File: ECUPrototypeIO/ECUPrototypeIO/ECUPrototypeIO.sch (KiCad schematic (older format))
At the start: 35 parts, among them SW2 MomentarySwitch, U1 LM358

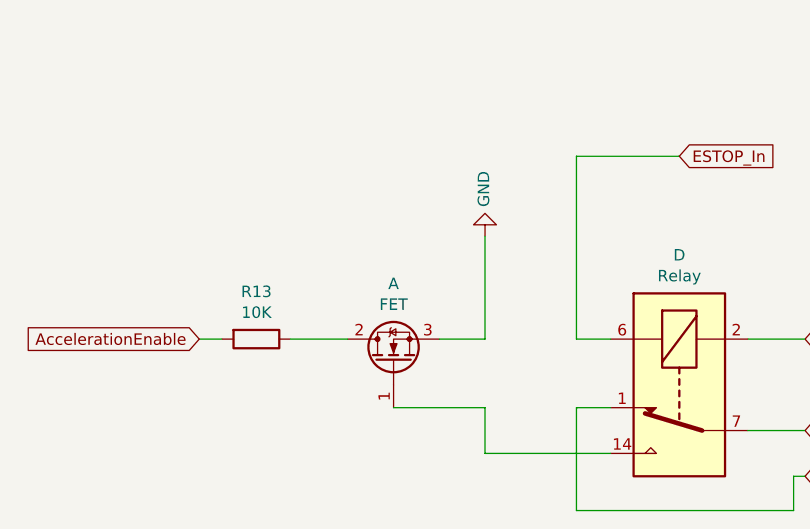
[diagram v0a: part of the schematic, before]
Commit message: Fixed the mosfet schematic
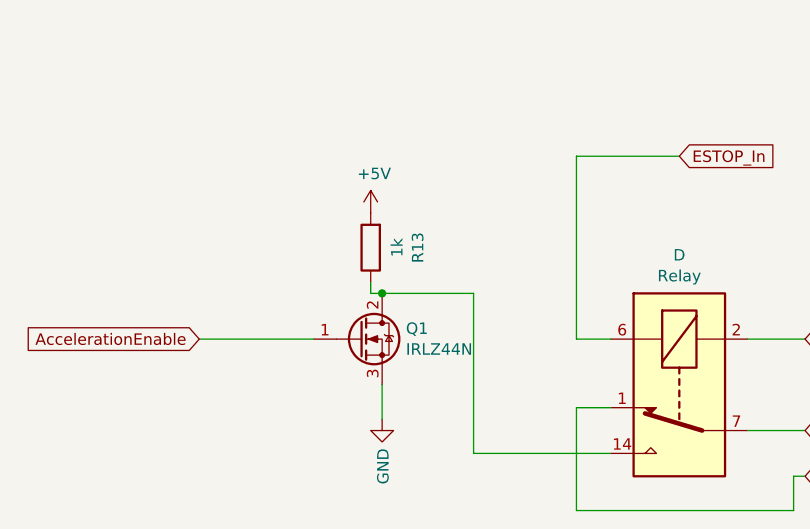
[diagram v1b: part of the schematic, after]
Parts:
- removed A: FET, Package_TO_SOT_THT:TO-220-3_Vertical, symbol Transistor_FET:IRF740
- added Q1: IRLZ44N, Package_TO_SOT_THT:TO-220-3_Vertical, symbol Transistor_FET:IRLZ44N
- R13: value 10K -> 1k
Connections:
- net labels added: +5V
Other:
- moved on the sheet: R13
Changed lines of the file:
@@
 L Device:R R13
 U 1 1 5E0710B8
-P 6950 8150
-F 0 "R13" V 6743 8150 50  0000 C CNN
-F 1 "10K" V 6834 8150 50  0000 C CNN
-F 2 "" V 6880 8150 50  0001 C CNN
-F 3 "~" H 6950 8150 50  0001 C CNN
-	1    6950 8150
-	0    1    1    0
+P 7450 7750
+F 0 "R13" V 7243 7750 50  0000 C CNN
+F 1 "1k" V 7334 7750 50  0000 C CNN
+F 2 "" V 7380 7750 50  0001 C CNN
+F 3 "~" H 7450 7750 50  0001 C CNN
+	1    7450 7750
+	-1   0    0    1
 $EndComp
 Text GLabel 6700 8150 0    50   Input ~ 0
 AccelerationEnable
-Wire Wire Line
-	6700 8150 6800 8150
 Text GLabel 8800 7350 2    50   Input ~ 0
 ESTOP_In
@@
 	8900 6450 9550 6450
 Connection ~ 8650 5750
-Wire Wire Line
-	7950 8650 8500 8650
 Text GLabel 9350 8550 2    50   Input ~ 0
 ACC_White
@@
 	11150 1450 11150 1300
 $Comp
-L Transistor_FET:IRF740 A
-U 1 1 5E2EE751
-P 7550 8250
-F 0 "A" V 7892 8250 50  0000 C CNN
-F 1 "FET" V 7801 8250 50  0000 C CNN
-F 2 "Package_TO_SOT_THT:TO-220-3_Vertical" H 7800 8175 50  0001 L CIN
-F 3 "http://www.vishay.com/docs/91054/91054.pdf" H 7550 8250 50  0001 L CNN
-	1    7550 8250
-	0    -1   -1   0
-$EndComp
-Wire Wire Line
-	7550 8450 7950 8450
-Wire Wire Line
-	7950 8450 7950 8650
-Wire Wire Line
-	7100 8150 7350 8150
-Wire Wire Line
-	7750 8150 7950 8150
-Wire Wire Line
-	7950 8150 7950 7700
-$Comp
 L power:GND #PWR?
 U 1 1 5E321D34
-P 7950 7700
-F 0 "#PWR?" H 7950 7450 50  0001 C CNN
-F 1 "GND" V 7955 7572 50  0000 R CNN
-F 2 "" H 7950 7700 50  0001 C CNN
-F 3 "" H 7950 7700 50  0001 C CNN
-	1    7950 7700
-	-1   0    0    1
-$EndComp
+P 7500 8500
+F 0 "#PWR?" H 7500 8250 50  0001 C CNN
+F 1 "GND" V 7505 8372 50  0000 R CNN
+F 2 "" H 7500 8500 50  0001 C CNN
+F 3 "" H 7500 8500 50  0001 C CNN
+	1    7500 8500
+	1    0    0    -1
+$EndComp
+$Comp
+L Transistor_FET:IRLZ44N Q1
+U 1 1 5E3F7CB4
+P 7400 8150
+F 0 "Q1" H 7604 8196 50  0000 L CNN
+F 1 "IRLZ44N" H 7604 8105 50  0000 L CNN
+F 2 "Package_TO_SOT_THT:TO-220-3_Vertical" H 7650 8075 50  0001 L CIN
+F 3 "http://www.irf.com/product-info/datasheets/data/irlz44n.pdf" H 7400 8150 50  0001 L CNN
+	1    7400 8150
+	1    0    0    -1
+$EndComp
+$Comp
+L power:+5V #PWR?
+U 1 1 5E421138
+P 7450 7600
+F 0 "#PWR?" H 7450 7450 50  0001 C CNN
+F 1 "+5V" H 7465 7773 50  0000 C CNN
+F 2 "" H 7450 7600 50  0001 C CNN
+F 3 "" H 7450 7600 50  0001 C CNN
+	1    7450 7600
+	1    0    0    -1
+$EndComp
+Wire Wire Line
+	6700 8150 7200 8150
+Wire Wire Line
+	7450 7900 7450 7950
+Wire Wire Line
+	7450 7950 7500 7950
+Connection ~ 7500 7950
+Wire Wire Line
+	7500 7950 7900 7950
+Wire Wire Line
+	7900 8650 8500 8650
+Wire Wire Line
+	7900 7950 7900 8650
+Wire Wire Line
+	7500 8350 7500 8500
 $EndSCHEMATC

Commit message: Not exactly sure what I changed.
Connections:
- wire segments 157 -> 156
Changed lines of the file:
@@
 Wire Wire Line
 	3550 3000 3900 3000
-Wire Wire Line
-	7050 6250 7000 6250
 Text GLabel 4500 1550 2    50   Input ~ 0
 RelayModuleGnd
